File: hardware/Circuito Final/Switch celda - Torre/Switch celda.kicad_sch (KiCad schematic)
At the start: 28 parts, among them Q1 MMBT2222A, Q2 MMBT2907A, Q3 MMBT2222A

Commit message: update pcb celdas
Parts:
- removed J_In_Out_1: Conn_02x04_Odd_Even, Connector_PinSocket_2.54mm:PinSocket_2x04_P2.54mm_Vertical, symbol Connector_Generic:Conn_02x04_Odd_Even
- removed J_In_cell_neg_1, Jumper_Vcell_1, Jumper_cell_neg_1: Conn_02x07_Odd_Even, Connector_PinSocket_2.54mm:PinSocket_2x07_P2.54mm_Vertical, symbol Connector_Generic:Conn_02x07_Odd_Even
- added H1, H2, H3, H4: MountingHole, MountingHole:MountingHole_3.5mm, symbol Mechanical:MountingHole
- added J_In_Out_1: Conn_01x04_Socket, symbol Connector:Conn_01x04_Socket
- added J_In_cell_neg_1: Conn_01x07_Socket, Connector_PinSocket_2.54mm:PinSocket_1x07_P2.54mm_Vertical, symbol Connector:Conn_01x07_Socket
- added Jumper_Vcell_1, Jumper_cell_neg_1: Conn_01x07_Pin, Connector_PinHeader_2.54mm:PinHeader_1x07_P2.54mm_Vertical, symbol Connector:Conn_01x07_Pin
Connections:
- net 0: now also J_In_Out_1.2 (Pin_2)
- net Vcc: now also J_In_Out_1.4 (Pin_4)
- net Vcell: now also Jumper_Vcell_1.1 (Pin_1), Jumper_Vcell_1.2 (Pin_2), Jumper_Vcell_1.3 (Pin_3), Jumper_Vcell_1.4 (Pin_4), Jumper_Vcell_1.5 (Pin_5), Jumper_Vcell_1.6 (Pin_6), Jumper_Vcell_1.7 (Pin_7)
- net Vcell_neg: now also Jumper_cell_neg_1.1 (Pin_1), Jumper_cell_neg_1.2 (Pin_2), Jumper_cell_neg_1.3 (Pin_3), Jumper_cell_neg_1.4 (Pin_4), Jumper_cell_neg_1.5 (Pin_5), Jumper_cell_neg_1.6 (Pin_6), Jumper_cell_neg_1.7 (Pin_7)
- net bus_neg: now also J_In_Out_1.1 (Pin_1)
- net bus_pos: now also J_In_Out_1.3 (Pin_3)
- net cell_neg1: now also J_In_cell_neg_1.1 (Pin_1)
- net cell_neg2: now also J_In_cell_neg_1.2 (Pin_2)
- net cell_neg3: now also J_In_cell_neg_1.3 (Pin_3)
- net cell_neg4: now also J_In_cell_neg_1.4 (Pin_4)
- net cell_neg5: now also J_In_cell_neg_1.5 (Pin_5)
- net cell_neg6: now also J_In_cell_neg_1.6 (Pin_6)
- net cell_neg7: now also J_In_cell_neg_1.7 (Pin_7)
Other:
- moved on the sheet: Rvia1

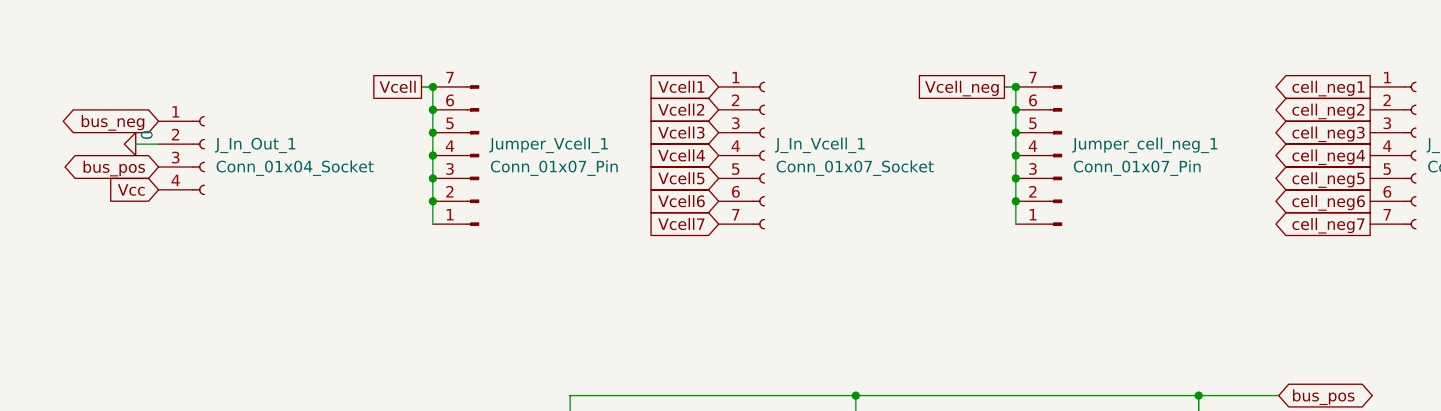
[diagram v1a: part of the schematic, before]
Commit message: PCB celda con los orificios para las varillas colocados y reduciendo la cantidad de pines hembra macho a la mitad
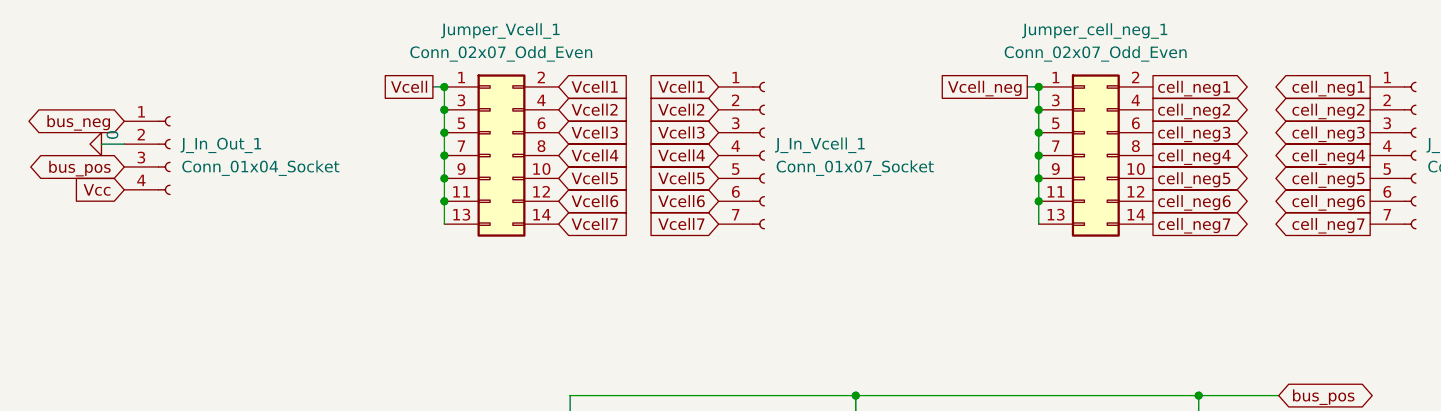
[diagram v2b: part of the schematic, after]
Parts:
- removed Jumper_Vcell_1, Jumper_cell_neg_1: Conn_01x07_Pin, Connector_PinHeader_2.54mm:PinHeader_1x07_P2.54mm_Vertical, symbol Connector:Conn_01x07_Pin
- added Jumper_Vcell_1, Jumper_cell_neg_1: Conn_02x07_Odd_Even, Connector_PinHeader_2.54mm:PinHeader_2x07_P2.54mm_Vertical, symbol Connector_Generic:Conn_02x07_Odd_Even
- J_In_Out_1: footprint (none) -> Connector_PinSocket_2.54mm:PinSocket_1x04_P2.54mm_Vertical
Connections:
- net Vcell: now also Jumper_Vcell_1.1 (Pin_1), Jumper_Vcell_1.11 (Pin_11), Jumper_Vcell_1.13 (Pin_13), Jumper_Vcell_1.3 (Pin_3), Jumper_Vcell_1.5 (Pin_5), Jumper_Vcell_1.7 (Pin_7), Jumper_Vcell_1.9 (Pin_9)
- net Vcell1: now also Jumper_Vcell_1.2 (Pin_2)
- net Vcell2: now also Jumper_Vcell_1.4 (Pin_4)
- net Vcell3: now also Jumper_Vcell_1.6 (Pin_6)
- net Vcell4: now also Jumper_Vcell_1.8 (Pin_8)
- net Vcell5: now also Jumper_Vcell_1.10 (Pin_10)
- net Vcell6: now also Jumper_Vcell_1.12 (Pin_12)
- net Vcell7: now also Jumper_Vcell_1.14 (Pin_14)
- net Vcell_neg: now also Jumper_cell_neg_1.1 (Pin_1), Jumper_cell_neg_1.11 (Pin_11), Jumper_cell_neg_1.13 (Pin_13), Jumper_cell_neg_1.3 (Pin_3), Jumper_cell_neg_1.5 (Pin_5), Jumper_cell_neg_1.7 (Pin_7), Jumper_cell_neg_1.9 (Pin_9)
- net cell_neg1: now also Jumper_cell_neg_1.2 (Pin_2)
- net cell_neg2: now also Jumper_cell_neg_1.4 (Pin_4)
- net cell_neg3: now also Jumper_cell_neg_1.6 (Pin_6)
- net cell_neg4: now also Jumper_cell_neg_1.8 (Pin_8)
- net cell_neg5: now also Jumper_cell_neg_1.10 (Pin_10)
- net cell_neg6: now also Jumper_cell_neg_1.12 (Pin_12)
- net cell_neg7: now also Jumper_cell_neg_1.14 (Pin_14)
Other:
- moved on the sheet: J_In_Out_1

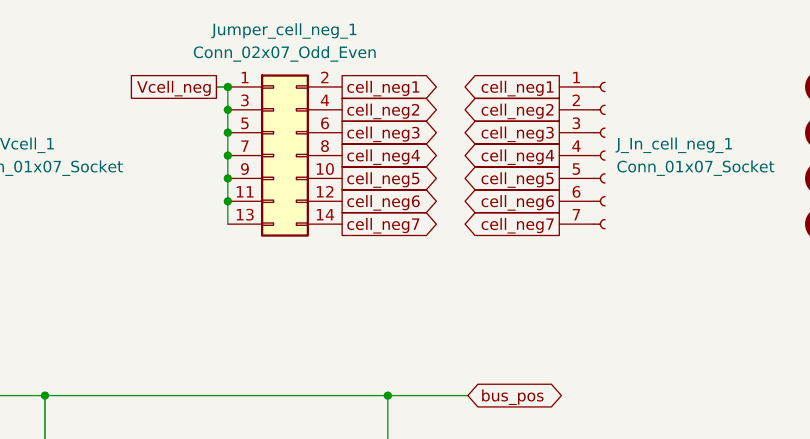
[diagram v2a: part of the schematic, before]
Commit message: update PCB celda con los modelos 3D corregidos
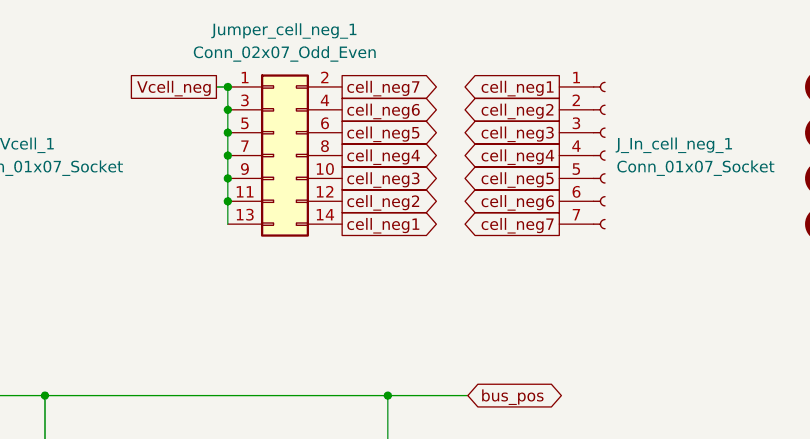
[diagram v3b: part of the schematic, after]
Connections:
- net cell_neg1: now also Jumper_cell_neg_1.14 (Pin_14); no longer Jumper_cell_neg_1.2 (Pin_2)
- net cell_neg2: now also Jumper_cell_neg_1.12 (Pin_12); no longer Jumper_cell_neg_1.4 (Pin_4)
- net cell_neg3: now also Jumper_cell_neg_1.10 (Pin_10); no longer Jumper_cell_neg_1.6 (Pin_6)
- net cell_neg5: now also Jumper_cell_neg_1.6 (Pin_6); no longer Jumper_cell_neg_1.10 (Pin_10)
- net cell_neg6: now also Jumper_cell_neg_1.4 (Pin_4); no longer Jumper_cell_neg_1.12 (Pin_12)
- net cell_neg7: now also Jumper_cell_neg_1.2 (Pin_2); no longer Jumper_cell_neg_1.14 (Pin_14)
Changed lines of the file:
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@@
-		)
-	)
-	(global_label "cell_neg2"
-		(shape output)
-		(at 151.13 24.13 0)
-		(fields_autoplaced yes)
-		(effects
-			(font
-				(size 1.27 1.27)
-			)
-			(justify left)
-		)
-		(property "Intersheetrefs" "${INTERSHEET_REFS}"
-			(at 163.1865 24.13 0)
-			(hide yes)
-			(show_name no)
-			(do_not_autoplace no)
-			(effects
-				(font
-					(size 1.27 1.27)
-				)
-				(justify left)
-			)
 		)
 	)
@@
 				)
 				(justify right)
+			)
+		)
+	)
+	(global_label "cell_neg5"
+		(shape output)
+		(at 151.13 26.67 0)
+		(fields_autoplaced yes)
+		(effects
+			(font
+				(size 1.27 1.27)
+			)
+			(justify left)
+		)
+		(property "Intersheetrefs" "${INTERSHEET_REFS}"
+			(at 163.1865 26.67 0)
+			(hide yes)
+			(show_name no)
+			(do_not_autoplace no)
+			(effects
+				(font
+					(size 1.27 1.27)
+				)
+				(justify left)
 			)
 		)
@@
 		)
 	)
-	(global_label "cell_neg1"
+	(global_label "cell_neg7"
 		(shape output)
 		(at 151.13 21.59 0)
@@
 		)
 	)
+	(global_label "cell_neg3"
+		(shape output)
+		(at 151.13 31.75 0)
+		(fields_autoplaced yes)
+		(effects
+			(font
+				(size 1.27 1.27)
+			)
+			(justify left)
+		)
+		(property "Intersheetrefs" "${INTERSHEET_REFS}"
+			(at 163.1865 31.75 0)
+			(hide yes)
+			(show_name no)
+			(do_not_autoplace no)
+			(effects
+				(font
+					(size 1.27 1.27)
+				)
+				(justify left)
+			)
+		)
+	)
 	(global_label "Vcell2"
 		(shape input)
@@
 		)
 	)
-	(global_label "cell_neg6"
-		(shape output)
-		(at 151.13 34.29 0)
-		(fields_autoplaced yes)
-		(effects
-			(font
-				(size 1.27 1.27)
-			)
-			(justify left)
-		)
-		(property "Intersheetrefs" "${INTERSHEET_REFS}"
-			(at 163.1865 34.29 0)
-			(hide yes)
-			(show_name no)
-			(do_not_autoplace no)
-			(effects
-				(font
-					(size 1.27 1.27)
-				)
-				(justify left)
-			)
-		)
-	)
 	(global_label "Vcell"
 		(shape passive)
@@
 		)
 	)
-	(global_label "cell_neg3"
-		(shape output)
-		(at 151.13 26.67 0)
-		(fields_autoplaced yes)
-		(effects
-			(font
-				(size 1.27 1.27)
-			)
-			(justify left)
-		)
-		(property "Intersheetrefs" "${INTERSHEET_REFS}"
-			(at 163.1865 26.67 0)
+	(global_label "cell_neg4"
+		(shape output)
+		(at 151.13 29.21 0)
+		(fields_autoplaced yes)
+		(effects
+			(font
+				(size 1.27 1.27)
+			)
+			(justify left)
+		)
+		(property "Intersheetrefs" "${INTERSHEET_REFS}"
+			(at 163.1865 29.21 0)
 			(hide yes)
 			(show_name no)
@@
 		)
 	)
-	(global_label "cell_neg4"
-		(shape output)
-		(at 151.13 29.21 0)
-		(fields_autoplaced yes)
-		(effects
-			(font
-				(size 1.27 1.27)
-			)
-			(justify left)
-		)
-		(property "Intersheetrefs" "${INTERSHEET_REFS}"
-			(at 163.1865 29.21 0)
-			(hide yes)
-			(show_name no)
-			(do_not_autoplace no)
-			(effects
-				(font
-					(size 1.27 1.27)
-				)
-				(justify left)
-			)
-		)
-	)
-	(global_label "cell_neg7"
+	(global_label "cell_neg6"
+		(shape output)
+		(at 151.13 24.13 0)
+		(fields_autoplaced yes)
+		(effects
+			(font
+				(size 1.27 1.27)
+			)
+			(justify left)
+		)
+		(property "Intersheetrefs" "${INTERSHEET_REFS}"
+			(at 163.1865 24.13 0)
+			(hide yes)
+			(show_name no)
+			(do_not_autoplace no)
+			(effects
+				(font
+					(size 1.27 1.27)
+				)
+				(justify left)
+			)
+		)
+	)
+	(global_label "cell_neg2"
+		(shape output)
+		(at 151.13 34.29 0)
+		(fields_autoplaced yes)
+		(effects
+			(font
+				(size 1.27 1.27)
+			)
+			(justify left)
+		)
+		(property "Intersheetrefs" "${INTERSHEET_REFS}"
+			(at 163.1865 34.29 0)
+			(hide yes)
+			(show_name no)
+			(do_not_autoplace no)
+			(effects
+				(font
+					(size 1.27 1.27)
+				)
+				(justify left)
+			)
+		)
+	)
+	(global_label "cell_neg1"
 		(shape output)
 		(at 151.13 36.83 0)
@@
 			(hide yes)
 			(show_name no)
-			(do_not_autoplace no)
-			(effects
-				(font
-					(size 1.27 1.27)
-				)
-				(justify left)
-			)
-		)
-	)
-	(global_label "cell_neg5"
-		(shape output)
-		(at 151.13 31.75 0)
-		(fields_autoplaced yes)
-		(effects
-			(font
-				(size 1.27 1.27)
-			)
-			(justify left)
-		)
-		(property "Intersheetrefs" "${INTERSHEET_REFS}"
-			(at 163.1865 31.75 0)
-			(hide yes)
-			(show_name no)

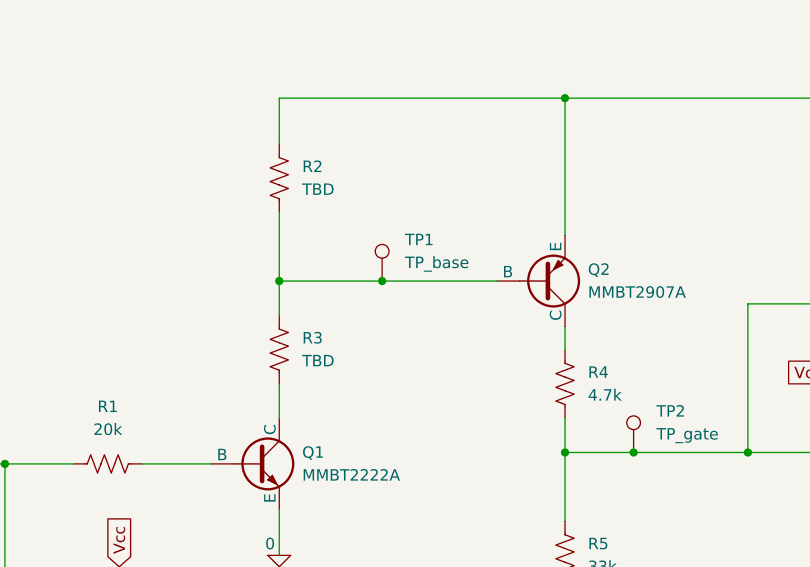
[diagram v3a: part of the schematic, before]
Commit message: subida version 2.2 del pcb de las celdas, junto con el modelo spice del TL084 y su datasheet
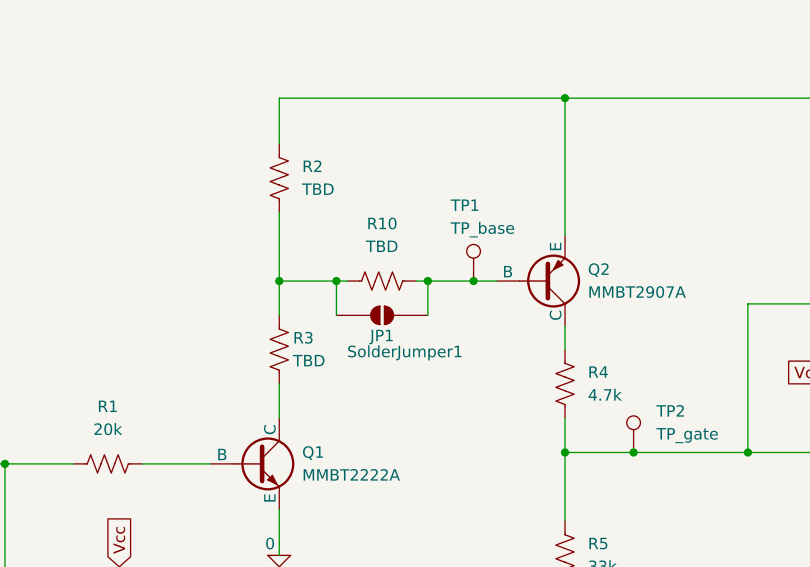
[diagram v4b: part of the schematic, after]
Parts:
- added JP1: SolderJumper1, Jumper:SolderJumper-2_P1.3mm_Open_TrianglePad1.0x1.5mm, symbol Jumper:SolderJumper_2_Open
- added R10: TBD, Resistor_SMD:R_1206_3216Metric_Pad1.30x1.75mm_HandSolder, symbol Device:R_US
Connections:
- net at R2.1, R3.2: now also JP1.1 (A), R10.1; no longer Q2.2 (B), TP1.1
- new net: JP1.2 (B), Q2.2 (B), R10.2, TP1.1
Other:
- moved on the sheet: TP1
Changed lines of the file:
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@@
 	)
 	(junction
+		(at 86.36 76.2)
+		(diameter 0)
+		(color 0 0 0 0)
+	)
+	(junction
 		(at 68.58 120.65)
 		(diameter 0)
@@
 	)
 	(junction
+		(at 107.95 76.2)
+		(diameter 0)
+		(color 0 0 0 0)
+	)
+	(junction
 		(at 72.39 21.59)
 		(diameter 0)
@@
 	)
 	(junction
+		(at 102.87 76.2)
+		(diameter 0)
+		(color 0 0 0 0)
+	)
+	(junction
 		(at 138.43 31.75)
 		(diameter 0)
@@
 	)
 	(junction
-		(at 138.43 26.67)
+		(at 92.71 76.2)
 		(diameter 0)
 		(color 0 0 0 0)
 	)
 	(junction
-		(at 72.39 34.29)
+		(at 138.43 26.67)
 		(diameter 0)
 		(color 0 0 0 0)
 	)
 	(junction
-		(at 72.39 26.67)
+		(at 72.39 34.29)
 		(diameter 0)
 		(color 0 0 0 0)
 	)
 	(junction
-		(at 138.43 29.21)
+		(at 72.39 26.67)
 		(diameter 0)
 		(color 0 0 0 0)
 	)
 	(junction
-		(at 97.79 76.2)
+		(at 138.43 29.21)
 		(diameter 0)
 		(color 0 0 0 0)
@@
 	)
 	(junction
-		(at 86.36 76.2)
-		(diameter 0)
-		(color 0 0 0 0)
-	)
-	(junction
 		(at 138.43 24.13)
 		(diameter 0)
@@
 	(wire
 		(pts
+			(xy 86.36 76.2) (xy 92.71 76.2)
+		)
+		(stroke
+			(width 0)
+			(type default)
+		)
+	)
+	(wire
+		(pts
 			(xy 228.6 69.85) (xy 228.6 73.66)
 		)
@@
 	(wire
 		(pts
+			(xy 92.71 76.2) (xy 92.71 80.01)
+		)
+		(stroke
+			(width 0)
+			(type default)
+		)
+	)
+	(wire
+		(pts
 			(xy 72.39 26.67) (xy 72.39 29.21)
 		)
@@
 	(wire
 		(pts
+			(xy 102.87 76.2) (xy 102.87 80.01)
+		)
+		(stroke
+			(width 0)
+			(type default)
+		)
+	)
+	(wire
+		(pts
 			(xy 118.11 110.49) (xy 118.11 115.57)
 		)
@@
 	(wire
 		(pts
+			(xy 101.6 76.2) (xy 102.87 76.2)
+		)
+		(stroke
+			(width 0)
+			(type default)
+		)
+	)
+	(wire
+		(pts
 			(xy 175.26 86.36) (xy 176.53 86.36)
 		)
@@
 	(wire
 		(pts
+			(xy 92.71 76.2) (xy 93.98 76.2)
+		)
+		(stroke
+			(width 0)
+			(type default)
+		)
+	)
+	(wire
+		(pts
 			(xy 68.58 120.65) (xy 68.58 121.92)
 		)
@@
 	(wire
 		(pts
-			(xy 86.36 76.2) (xy 97.79 76.2)
+			(xy 102.87 76.2) (xy 107.95 76.2)
 		)
 		(stroke
@@
 	(wire
 		(pts
-			(xy 86.36 68.58) (xy 86.36 76.2)
+			(xy 118.11 55.88) (xy 86.36 55.88)
 		)
 		(stroke
@@
 	(wire
 		(pts
-			(xy 118.11 55.88) (xy 86.36 55.88)
+			(xy 137.16 21.59) (xy 138.43 21.59)
 		)
 		(stroke
@@
 	(wire
 		(pts
-			(xy 137.16 21.59) (xy 138.43 21.59)
+			(xy 138.43 78.74) (xy 138.43 95.25)
 		)
 		(stroke
@@
 	(wire
 		(pts
-			(xy 138.43 78.74) (xy 138.43 95.25)
+			(xy 71.12 21.59) (xy 72.39 21.59)
 		)
 		(stroke
@@
 	(wire
 		(pts
-			(xy 71.12 21.59) (xy 72.39 21.59)
+			(xy 72.39 31.75) (xy 72.39 34.29)
 		)
 		(stroke
@@
 	(wire
 		(pts
-			(xy 72.39 31.75) (xy 72.39 34.29)
+			(xy 138.43 34.29) (xy 138.43 36.83)
 		)
 		(stroke
@@
 	(wire
 		(pts
-			(xy 138.43 34.29) (xy 138.43 36.83)
+			(xy 107.95 76.2) (xy 110.49 76.2)
 		)
 		(stroke
@@
 	(wire
 		(pts
-			(xy 97.79 76.2) (xy 110.49 76.2)
+			(xy 86.36 76.2) (xy 86.36 80.01)
 		)
 		(stroke
@@
 	(wire
 		(pts
-			(xy 86.36 76.2) (xy 86.36 80.01)
+			(xy 86.36 68.58) (xy 86.36 76.2)
 		)
 		(stroke
@@
 	)
 	(symbol
+		(lib_id "Jumper:SolderJumper_2_Open")
+		(at 97.79 80.01 0)
+		(unit 1)
+		(body_style 1)
+		(exclude_from_sim no)
+		(in_bom no)
+		(on_board yes)
+		(in_pos_files yes)
+		(dnp no)
+		(property "Reference" "JP1"
+			(at 97.79 82.296 0)
+			(show_name no)
+			(do_not_autoplace no)
+			(effects
+				(font
+					(size 1.27 1.27)
+				)
+			)
+		)
+		(property "Value" "SolderJumper1"
+			(at 100.33 84.074 0)
+			(show_name no)
+			(do_not_autoplace no)
+			(effects
+				(font
+					(size 1.27 1.27)
+				)
+			)
+		)
+		(property "Footprint" "Jumper:SolderJumper-2_P1.3mm_Open_TrianglePad1.0x1.5mm"
+			(at 97.79 80.01 0)
+			(hide yes)
+			(show_name no)
+			(do_not_autoplace no)
+			(effects
+				(font
+					(size 1.27 1.27)
+				)
+			)
+		)
+		(property "Datasheet" ""
+			(at 97.79 87.63 0)
+			(hide yes)
+			(show_name no)
+			(do_not_autoplace no)
+			(effects
+				(font
+					(size 1.27 1.27)
+				)
+			)
+		)
+		(property "Description" "Solder Jumper, 2-pole, open"
+			(at 97.79 85.09 0)
+			(hide yes)
+			(show_name no)
+			(do_not_autoplace no)
+			(effects
+				(font
+					(size 1.27 1.27)
+				)
+			)
+		)
+		(pin "1"
+		)
+		(pin "2"
+		)
+		(instances
+			(project "Switch celda"
+				(path "/4783565b-68b0-4d0c-b0f9-91a8fe34107e"
+					(reference "JP1")
+					(unit 1)
+				)
+			)
+		)
+	)
+	(symbol
 		(lib_id "Simulation_SPICE:NPN")
 		(at 83.82 96.52 0)
@@
 		(in_pos_files yes)
 		(dnp no)
-		(fields_autoplaced yes)
 		(property "Reference" "R3"
-			(at 88.9 82.5499 0)
+			(at 87.884 82.55 0)
 			(show_name no)
 			(do_not_autoplace no)
@@
 		)
 		(property "Value" "TBD"
-			(at 88.9 85.0899 0)
+			(at 87.884 85.09 0)
 			(show_name no)
 			(do_not_autoplace no)
@@
 	)
 	(symbol
+		(lib_id "Device:R_US")
+		(at 97.79 76.2 90)
+		(unit 1)
+		(body_style 1)
+		(exclude_from_sim no)
+		(in_bom yes)
+		(on_board yes)
+		(in_pos_files yes)
+		(dnp no)
+		(fields_autoplaced yes)
+		(property "Reference" "R10"
+			(at 97.79 69.85 90)
+			(show_name no)
+			(do_not_autoplace no)
+			(effects
+				(font
+					(size 1.27 1.27)
+				)
+			)
+		)
+		(property "Value" "TBD"
+			(at 97.79 72.39 90)
+			(show_name no)
+			(do_not_autoplace no)
+			(effects
+				(font
+					(size 1.27 1.27)
+				)
+			)
+		)
+		(property "Footprint" "Resistor_SMD:R_1206_3216Metric_Pad1.30x1.75mm_HandSolder"
+			(at 98.044 75.184 90)
+			(hide yes)
+			(show_name no)
+			(do_not_autoplace no)
+			(effects
+				(font
+					(size 1.27 1.27)
+				)
+			)
+		)
+		(property "Datasheet" ""
+			(at 97.79 76.2 0)
+			(hide yes)
+			(show_name no)
+			(do_not_autoplace no)
+			(effects
+				(font
+					(size 1.27 1.27)
+				)
+			)
+		)
+		(property "Description" "Resistor, US symbol"
+			(at 97.79 76.2 0)
+			(hide yes)
+			(show_name no)
+			(do_not_autoplace no)
+			(effects
+				(font
+					(size 1.27 1.27)
+				)
+			)
+		)
+		(pin "2"
+		)
+		(pin "1"
+		)
+		(instances
+			(project "Switch celda"
+				(path "/4783565b-68b0-4d0c-b0f9-91a8fe34107e"
+					(reference "R10")
+					(unit 1)
+				)
+			)
+		)
+	)
+	(symbol
 		(lib_id "Simulation_SPICE:PNP")
 		(at 115.57 76.2 0)
@@
 	(symbol
 		(lib_id "Connector:TestPoint")
-		(at 97.79 76.2 0)
+		(at 107.95 76.2 0)
 		(unit 1)
 		(body_style 1)
@@
 		(in_pos_files yes)
 		(dnp no)
-		(fields_autoplaced yes)
 		(property "Reference" "TP1"
-			(at 100.33 71.6279 0)
+			(at 105.41 67.818 0)
 			(show_name no)
 			(do_not_autoplace no)
@@
 		)
 		(property "Value" "TP_base"
-			(at 100.33 74.1679 0)
+			(at 105.41 70.358 0)
 			(show_name no)
 			(do_not_autoplace no)
@@
 		)
 		(property "Footprint" "TestPoint:TestPoint_Loop_D2.54mm_Drill1.5mm_Beaded"
-			(at 102.87 76.2 0)
+			(at 113.03 76.2 0)
 			(hide yes)
 			(show_name no)
@@
 		)
 		(property "Datasheet" "https://datasheet.octopart.com/5001-Keystone-datasheet-7268890.pdf"
-			(at 102.87 76.2 0)
+			(at 113.03 76.2 0)
 			(hide yes)
 			(show_name no)
@@
 		)
 		(property "Description" "test point"
-			(at 97.79 76.2 0)
+			(at 107.95 76.2 0)
 			(hide yes)
 			(show_name no)
